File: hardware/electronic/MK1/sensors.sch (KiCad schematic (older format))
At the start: 5 parts

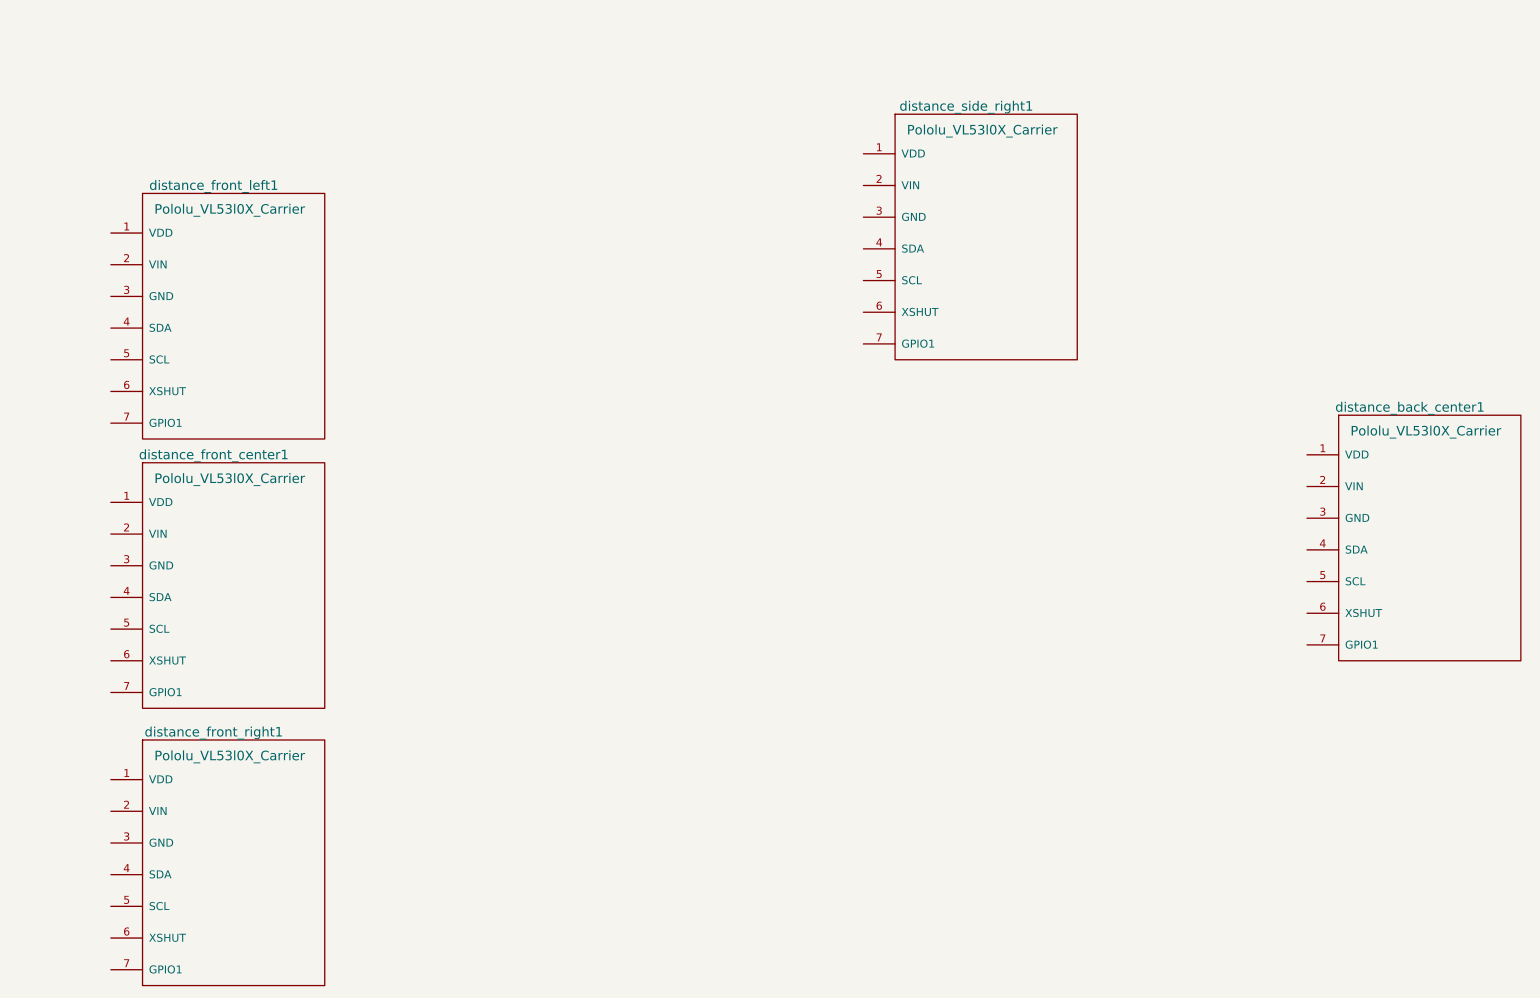
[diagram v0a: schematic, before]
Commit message: HW: Add sensors wiring
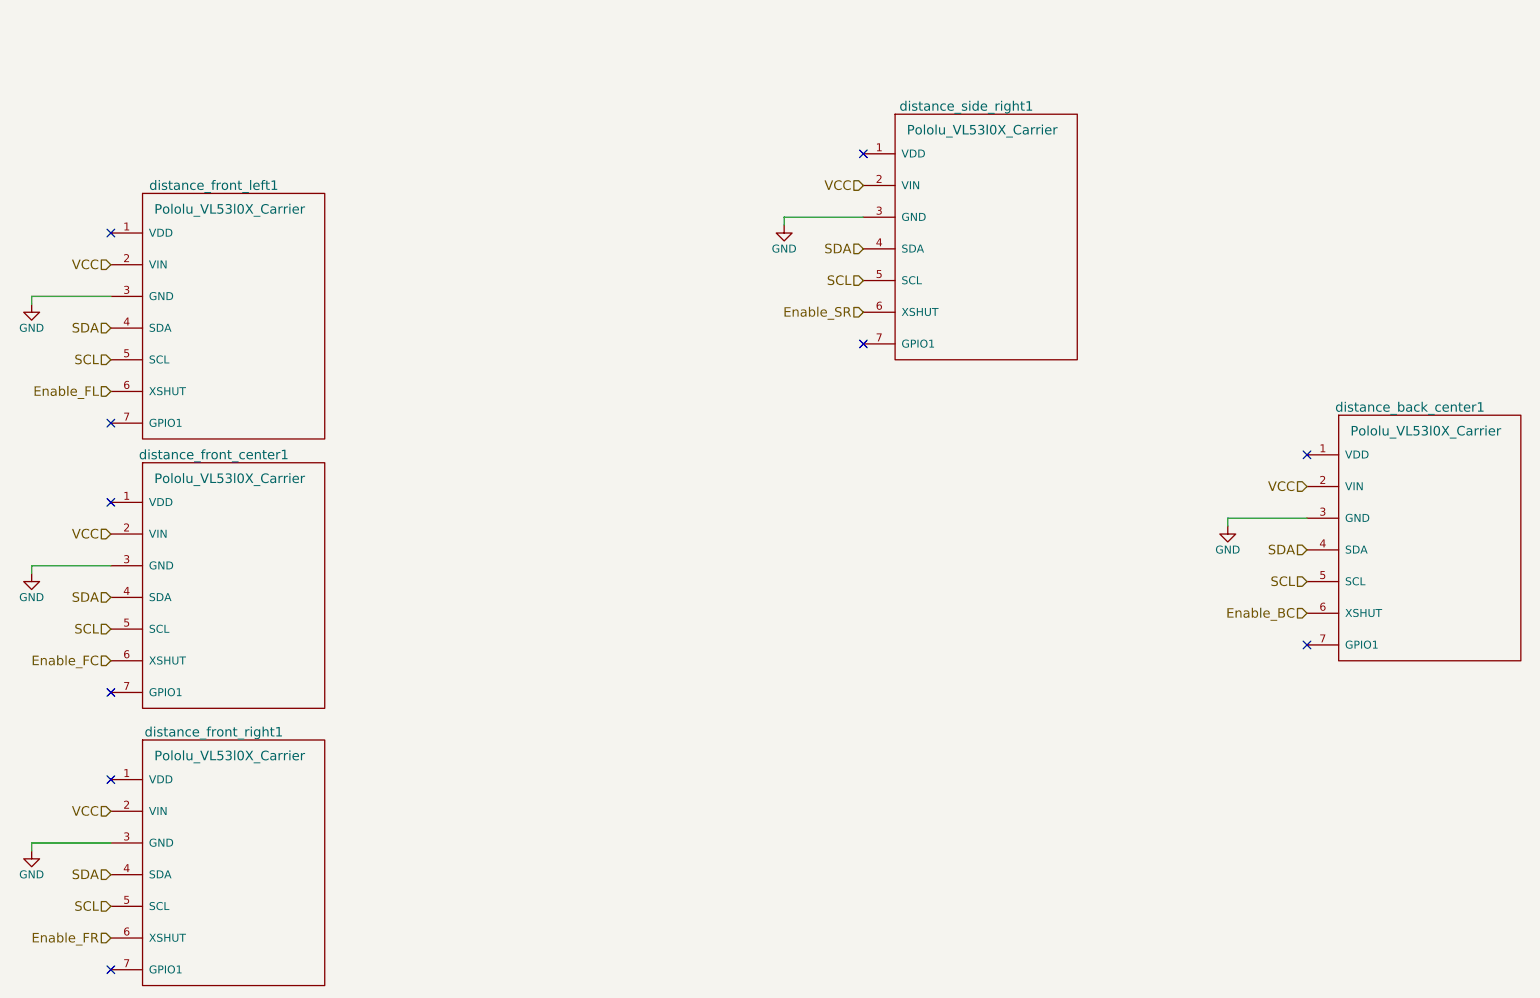
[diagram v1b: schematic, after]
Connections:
- net VCC: now reaches distance_front_center1.2 (VIN)
- net VCC: now also distance_back_center1.2 (VIN), distance_front_left1.2 (VIN), distance_front_right1.2 (VIN), distance_side_right1.2 (VIN)
- net GND: now reaches distance_front_center1.3 (GND)
- net GND: now also distance_back_center1.3 (GND), distance_front_left1.3 (GND), distance_front_right1.3 (GND), distance_side_right1.3 (GND)
- net SDA: now reaches distance_front_center1.4 (SDA)
- net SDA: now also distance_back_center1.4 (SDA), distance_front_left1.4 (SDA), distance_front_right1.4 (SDA), distance_side_right1.4 (SDA)
- net SCL: now reaches distance_front_center1.5 (SCL)
- net SCL: now also distance_back_center1.5 (SCL), distance_front_left1.5 (SCL), distance_front_right1.5 (SCL), distance_side_right1.5 (SCL)
- net Enable_FC: now reaches distance_front_center1.6 (XSHUT)
- net Enable_FR: now reaches distance_front_right1.6 (XSHUT)
- net Enable_FL: now reaches distance_front_left1.6 (XSHUT)
- net Enable_BC: now reaches distance_back_center1.6 (XSHUT)
- net Enable_SR: now reaches distance_side_right1.6 (XSHUT)
- no-connect marks 0 -> 10
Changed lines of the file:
@@
 	1    0    0    -1
 $EndComp
+Text HLabel 1550 2150 0    60   Input ~ 0
+VCC
+Text HLabel 1550 3850 0    60   Input ~ 0
+VCC
+Text HLabel 1550 5600 0    60   Input ~ 0
+VCC
+Text HLabel 6300 1650 0    60   Input ~ 0
+VCC
+Text HLabel 9100 3550 0    60   Input ~ 0
+VCC
+NoConn ~ 9100 3350
+NoConn ~ 6300 1450
+NoConn ~ 1550 1950
+NoConn ~ 1550 3650
+NoConn ~ 1550 5400
+NoConn ~ 1550 4850
+NoConn ~ 1550 6600
+NoConn ~ 1550 3150
+NoConn ~ 6300 2650
+NoConn ~ 9100 4550
+Text HLabel 1550 6000 0    60   Input ~ 0
+SDA
+Text HLabel 1550 6200 0    60   Input ~ 0
+SCL
+Wire Wire Line
+	1550 5800 1050 5800
+Wire Wire Line
+	1050 5800 1050 5850
+$Comp
+L GND #PWR?
+U 1 1 588B46A8
+P 1050 5850
+F 0 "#PWR?" H 1050 5600 50  0001 C CNN
+F 1 "GND" H 1050 5700 50  0000 C CNN
+F 2 "" H 1050 5850 50  0000 C CNN
+F 3 "" H 1050 5850 50  0000 C CNN
+	1    1050 5850
+	1    0    0    -1
+$EndComp
+Text HLabel 1550 4250 0    60   Input ~ 0
+SDA
+Text HLabel 1550 4450 0    60   Input ~ 0
+SCL
+Wire Wire Line
+	1550 4050 1050 4050
+Wire Wire Line
+	1050 4050 1050 4100
+$Comp
+L GND #PWR?
+U 1 1 588B4727
+P 1050 4100
+F 0 "#PWR?" H 1050 3850 50  0001 C CNN
+F 1 "GND" H 1050 3950 50  0000 C CNN
+F 2 "" H 1050 4100 50  0000 C CNN
+F 3 "" H 1050 4100 50  0000 C CNN
+	1    1050 4100
+	1    0    0    -1
+$EndComp
+Text HLabel 1550 2550 0    60   Input ~ 0
+SDA
+Text HLabel 1550 2750 0    60   Input ~ 0
+SCL
+Wire Wire Line
+	1550 2350 1050 2350
+Wire Wire Line
+	1050 2350 1050 2400
+$Comp
+L GND #PWR?
+U 1 1 588B479C
+P 1050 2400
+F 0 "#PWR?" H 1050 2150 50  0001 C CNN
+F 1 "GND" H 1050 2250 50  0000 C CNN
+F 2 "" H 1050 2400 50  0000 C CNN
+F 3 "" H 1050 2400 50  0000 C CNN
+	1    1050 2400
+	1    0    0    -1
+$EndComp
+Text HLabel 6300 2050 0    60   Input ~ 0
+SDA
+Text HLabel 6300 2250 0    60   Input ~ 0
+SCL
+Wire Wire Line
+	6300 1850 5800 1850
+Wire Wire Line
+	5800 1850 5800 1900
+$Comp
+L GND #PWR?
+U 1 1 588B483E
+P 5800 1900
+F 0 "#PWR?" H 5800 1650 50  0001 C CNN
+F 1 "GND" H 5800 1750 50  0000 C CNN
+F 2 "" H 5800 1900 50  0000 C CNN
+F 3 "" H 5800 1900 50  0000 C CNN
+	1    5800 1900
+	1    0    0    -1
+$EndComp
+Text HLabel 9100 3950 0    60   Input ~ 0
+SDA
+Text HLabel 9100 4150 0    60   Input ~ 0
+SCL
+Wire Wire Line
+	9100 3750 8600 3750
+Wire Wire Line
+	8600 3750 8600 3800
+$Comp
+L GND #PWR?
+U 1 1 588B4912
+P 8600 3800
+F 0 "#PWR?" H 8600 3550 50  0001 C CNN
+F 1 "GND" H 8600 3650 50  0000 C CNN
+F 2 "" H 8600 3800 50  0000 C CNN
+F 3 "" H 8600 3800 50  0000 C CNN
+	1    8600 3800
+	1    0    0    -1
+$EndComp
+Text HLabel 1550 2950 0    60   Input ~ 0
+Enable_FL
+Text HLabel 1550 4650 0    60   Input ~ 0
+Enable_FC
+Text HLabel 1550 6400 0    60   Input ~ 0
+Enable_FR
+Text HLabel 6300 2450 0    60   Input ~ 0
+Enable_SR
+Text HLabel 9100 4350 0    60   Input ~ 0
+Enable_BC
 $EndSCHEMATC

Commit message: HW: Minor cleanup in the schematics and layout
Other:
- note added: "Distance sensors"
- moved on the sheet: distance_side_right1
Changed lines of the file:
@@
 encoding utf-8
 Sheet 6 7
-Title ""
+Title "O'PAVES Mk-I"
 Date ""
-Rev ""
-Comp ""
+Rev "A"
+Comp "AdaCore"
 Comment1 ""
 Comment2 ""
@@
 L Pololu_VL53l0X_Carrier distance_side_right1
 U 1 1 5886C9C5
-P 6500 1200
-F 0 "distance_side_right1" H 6950 1250 60  0000 C CNN
-F 1 "Pololu_VL53l0X_Carrier" H 7050 1100 60  0000 C CNN
-F 2 "OPAVES_Footprints:Pololu_VL53L0x_Carrier" H 6500 1150 60  0001 C CNN
-F 3 "" H 6500 1150 60  0001 C CNN
-	1    6500 1200
+P 6500 1650
+F 0 "distance_side_right1" H 6950 1700 60  0000 C CNN
+F 1 "Pololu_VL53l0X_Carrier" H 7050 1550 60  0000 C CNN
+F 2 "OPAVES_Footprints:Pololu_VL53L0x_Carrier" H 6500 1600 60  0001 C CNN
+F 3 "" H 6500 1600 60  0001 C CNN
+	1    6500 1650
 	1    0    0    -1
 $EndComp
@@
 Text HLabel 1550 5600 0    60   Input ~ 0
 VCC
-Text HLabel 6300 1650 0    60   Input ~ 0
+Text HLabel 6300 2100 0    60   Input ~ 0
 VCC
 Text HLabel 9100 3550 0    60   Input ~ 0
 VCC
 NoConn ~ 9100 3350
-NoConn ~ 6300 1450
+NoConn ~ 6300 1900
 NoConn ~ 1550 1950
 NoConn ~ 1550 3650
@@
 NoConn ~ 1550 6600
 NoConn ~ 1550 3150
-NoConn ~ 6300 2650
+NoConn ~ 6300 3100
 NoConn ~ 9100 4550
 Text HLabel 1550 6000 0    60   Input ~ 0
@@
 	1    0    0    -1
 $EndComp
-Text HLabel 6300 2050 0    60   Input ~ 0
+Text HLabel 6300 2500 0    60   Input ~ 0
 SDA
-Text HLabel 6300 2250 0    60   Input ~ 0
+Text HLabel 6300 2700 0    60   Input ~ 0
 SCL
 Wire Wire Line
-	6300 1850 5800 1850
+	6300 2300 5800 2300
 Wire Wire Line
-	5800 1850 5800 1900
+	5800 2300 5800 2350
 $Comp
 L GND #PWR027
 U 1 1 588B483E
-P 5800 1900
-F 0 "#PWR027" H 5800 1650 50  0001 C CNN
-F 1 "GND" H 5800 1750 50  0000 C CNN
-F 2 "" H 5800 1900 50  0000 C CNN
-F 3 "" H 5800 1900 50  0000 C CNN
-	1    5800 1900
+P 5800 2350
+F 0 "#PWR027" H 5800 2100 50  0001 C CNN
+F 1 "GND" H 5800 2200 50  0000 C CNN
+F 2 "" H 5800 2350 50  0000 C CNN
+F 3 "" H 5800 2350 50  0000 C CNN
+	1    5800 2350
 	1    0    0    -1
 $EndComp
@@
 Text HLabel 1550 6400 0    60   Input ~ 0
 Enable_FR
-Text HLabel 6300 2450 0    60   Input ~ 0
+Text HLabel 6300 2900 0    60   Input ~ 0
 Enable_SR
 Text HLabel 9100 4350 0    60   Input ~ 0
 Enable_BC
+Text Notes 4400 950  0    236  ~ 0
+Distance sensors
 $EndSCHEMATC
